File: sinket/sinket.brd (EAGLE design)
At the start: 36 x 36 mm, 26 parts, among them IC1 ATTINY85-20PU, IC2 TS2940CP50S

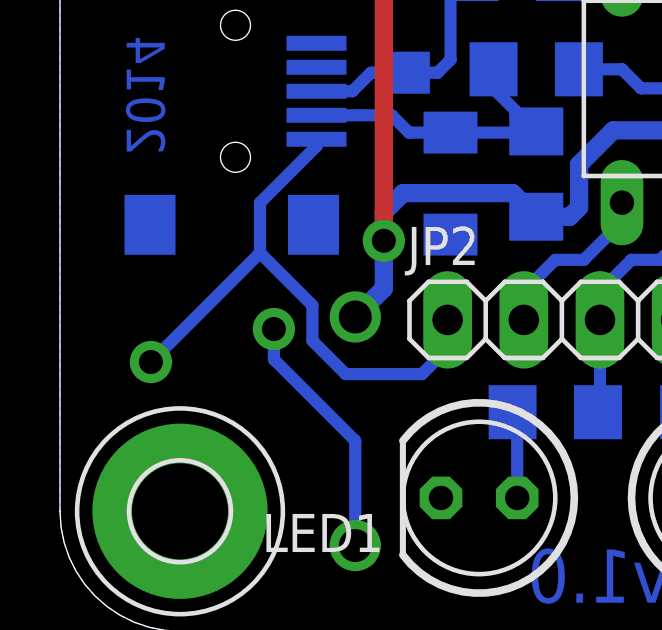
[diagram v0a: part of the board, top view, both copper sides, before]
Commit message: move fuse away from mounting hole
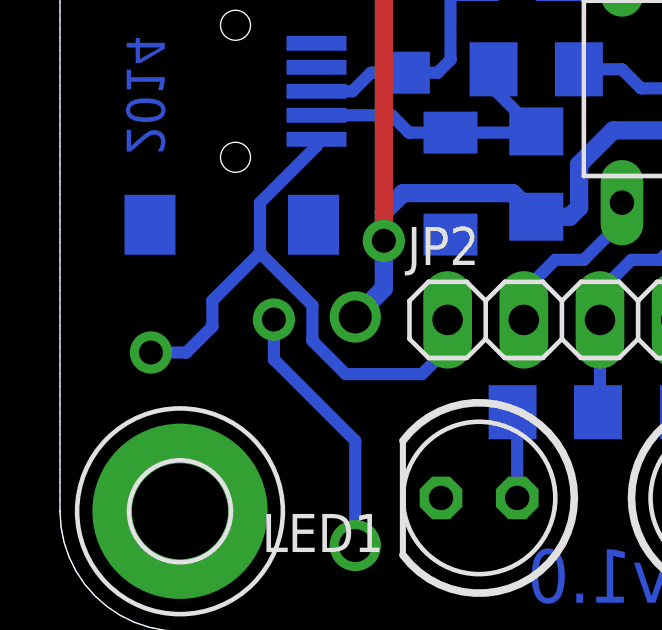
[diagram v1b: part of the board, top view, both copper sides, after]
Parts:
- moved F1 0.32 mm to (5.08, 9.84)
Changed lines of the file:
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@@
 <element name="C2" library="rcl" package="C025-030X050" value="470n" x="6.985" y="25.7175" rot="R180"/>
 <element name="C3" library="rcl" package="E2,5-6" value="47u" x="12.3825" y="32.0675" rot="R270"/>
-<element name="F1" library="n39" package="LP60-050" value="500mA" x="5.08" y="9.525" rot="MR180"/>
+<element name="F1" library="n39" package="LP60-050" value="500mA" x="5.08" y="9.8425" rot="MR180"/>
 <element name="U$7" library="n39" package="RIACON_101_2" value="RIACON_101_2" x="32.0675" y="22.5425" rot="R90">
 <attribute name="REICHELT" value="AKL 101-02" x="32.0675" y="22.5425" size="1.778" layer="27" rot="R90" display="off"/>
@@
 <wire x1="8.55" y1="16.17" x2="6.6675" y2="14.2875" width="0.4064" layer="16"/>
 <wire x1="6.6675" y1="14.2875" x2="6.6675" y2="12.6125" width="0.4064" layer="16"/>
-<wire x1="6.6675" y1="12.6125" x2="3.03" y2="8.975" width="0.4064" layer="16"/>
 <wire x1="12.92" y1="10.38" x2="12.92" y2="9.4275" width="0.4064" layer="16"/>
 <wire x1="12.92" y1="9.4275" x2="12.065" y2="8.5725" width="0.4064" layer="16"/>
@@
 <wire x1="8.41375" y1="9.68375" x2="8.41375" y2="10.86625" width="0.4064" layer="16"/>
 <wire x1="8.41375" y1="10.86625" x2="6.6675" y2="12.6125" width="0.4064" layer="16"/>
+<wire x1="6.6675" y1="12.6125" x2="5.08" y2="11.025" width="0.4064" layer="16"/>
+<wire x1="5.08" y1="11.025" x2="5.08" y2="10.16" width="0.4064" layer="16"/>
+<wire x1="3.03" y1="9.2925" x2="4.2125" y2="9.2925" width="0.4064" layer="16"/>
+<wire x1="4.2125" y1="9.2925" x2="5.08" y2="10.16" width="0.4064" layer="16"/>
 </signal>
 <signal name="GND" class="1">
@@
 <contactref element="F1" pad="P$2"/>
 <contactref element="D3" pad="A"/>
-<wire x1="7.13" y1="10.075" x2="7.13" y2="9.0625" width="0.4064" layer="16"/>
+<wire x1="7.13" y1="10.3925" x2="7.13" y2="9.0625" width="0.4064" layer="16"/>
 <wire x1="7.13" y1="9.0625" x2="9.8425" y2="6.35" width="0.4064" layer="16"/>
 <wire x1="9.8425" y1="6.35" x2="9.8425" y2="2.8575" width="0.4064" layer="16"/>
